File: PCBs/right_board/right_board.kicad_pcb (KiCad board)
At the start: 2 copper layers, 143.8 x 139.6 mm, 98 parts, among them J101 USB4510-03-1-A, J102 Conn_ARM_SWD_TagConnect_TC2030, J103 GSB12J21C1EU, J104 USB4510-03-1-A, SW101 SW_DIP_x01, SW102 SW_DIP_x01, SW103 SW_DIP_x01, SW104 SW_DIP_x01, SW105 SW_DIP_x01, SW106 SW_DIP_x01, SW107 SW_DIP_x01, SW108 SW_DIP_x01, SW109 SW_DIP_x01, SW110 SW_DIP_x01, SW111 SW_DIP_x01, SW112 SW_DIP_x01, SW113 SW_DIP_x01, SW114 SW_DIP_x01, SW115 SW_DIP_x01, SW116 SW_DIP_x01, SW117 SW_DIP_x01, SW118 SW_DIP_x01, SW119 SW_DIP_x01, SW120 SW_DIP_x01, SW121 SW_DIP_x01, SW122 SW_DIP_x01, SW123 SW_DIP_x01, SW124 SW_DIP_x01, SW125 SW_DIP_x01, SW126 SW_DIP_x01, SW127 SW_DIP_x01, SW128 RIC11-31S15.5D7-TH, U101 STM32G0C1CEUx, U102 USB2533-1080AEN, U103 M24256X-FCU6T_VF, U104 USBLC6-4SC6, U105 USBLC6-4SC6, U106 USBLC6-4SC6, Y101 CX2016SA24000D0HLLG3

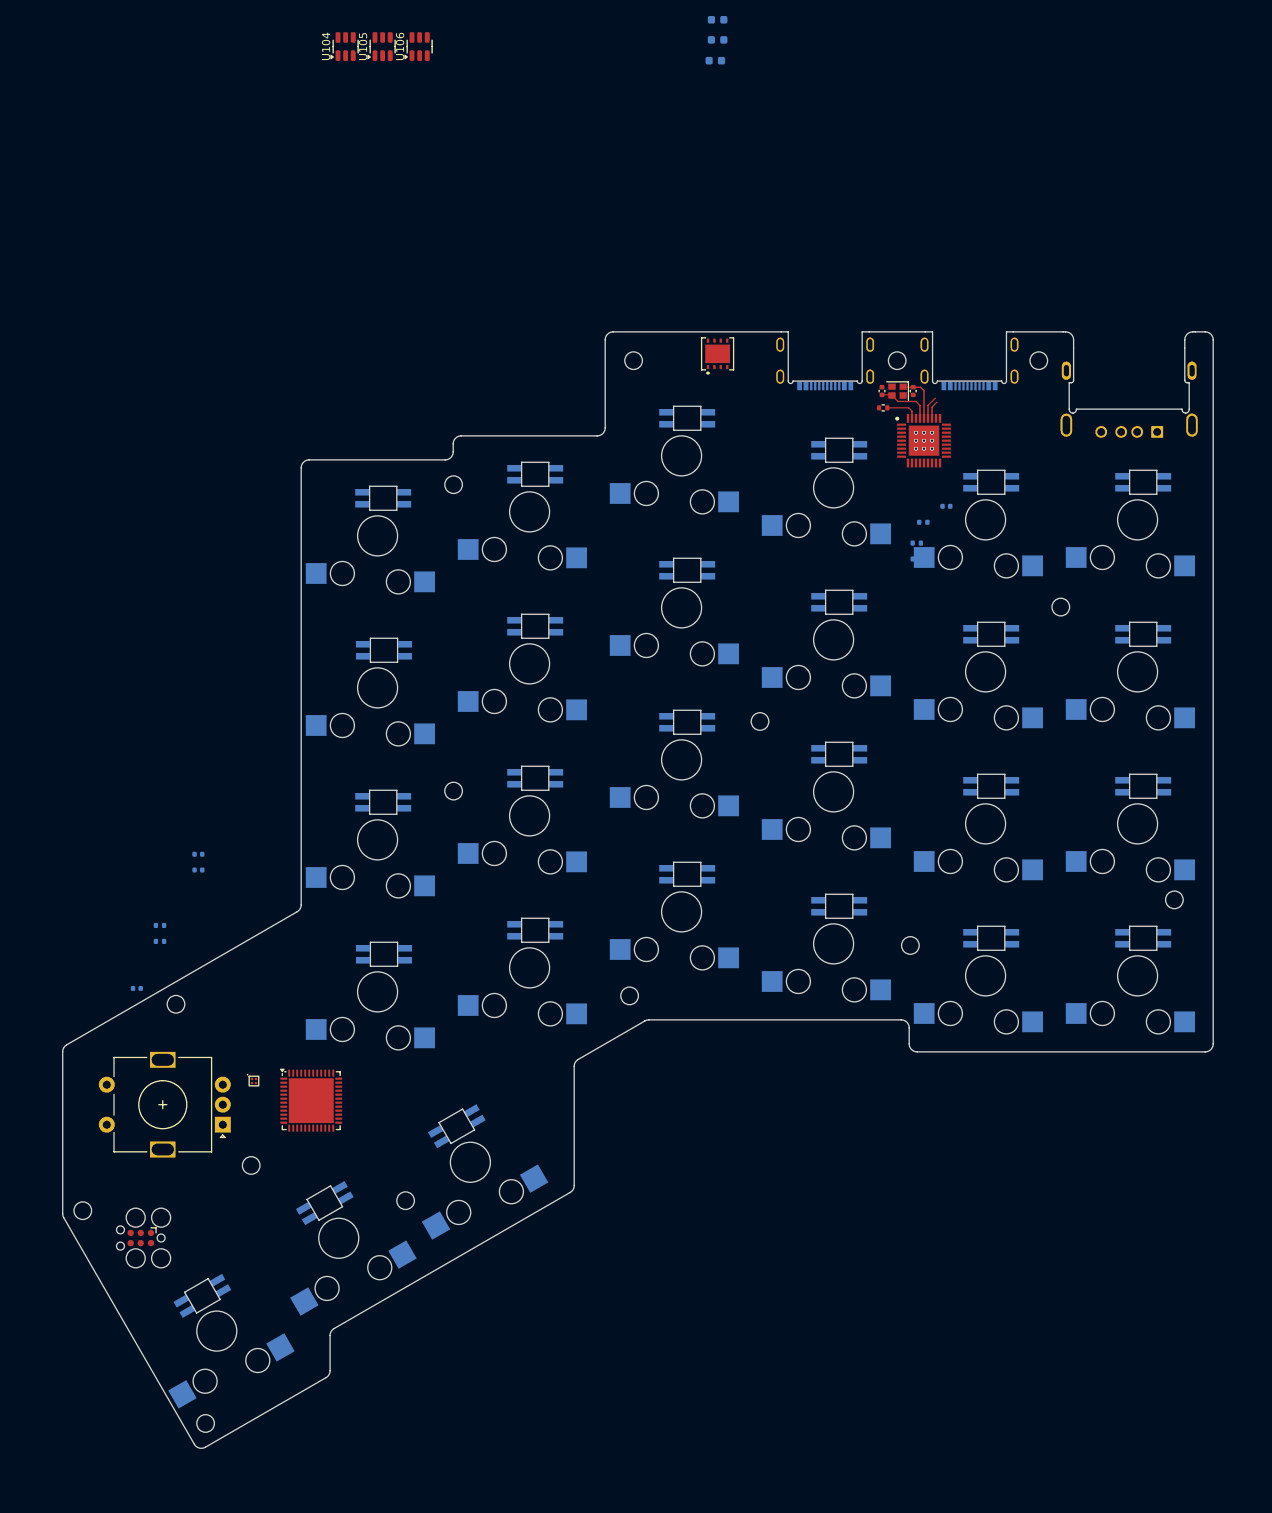
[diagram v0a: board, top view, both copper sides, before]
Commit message: Right board done, all components ordered
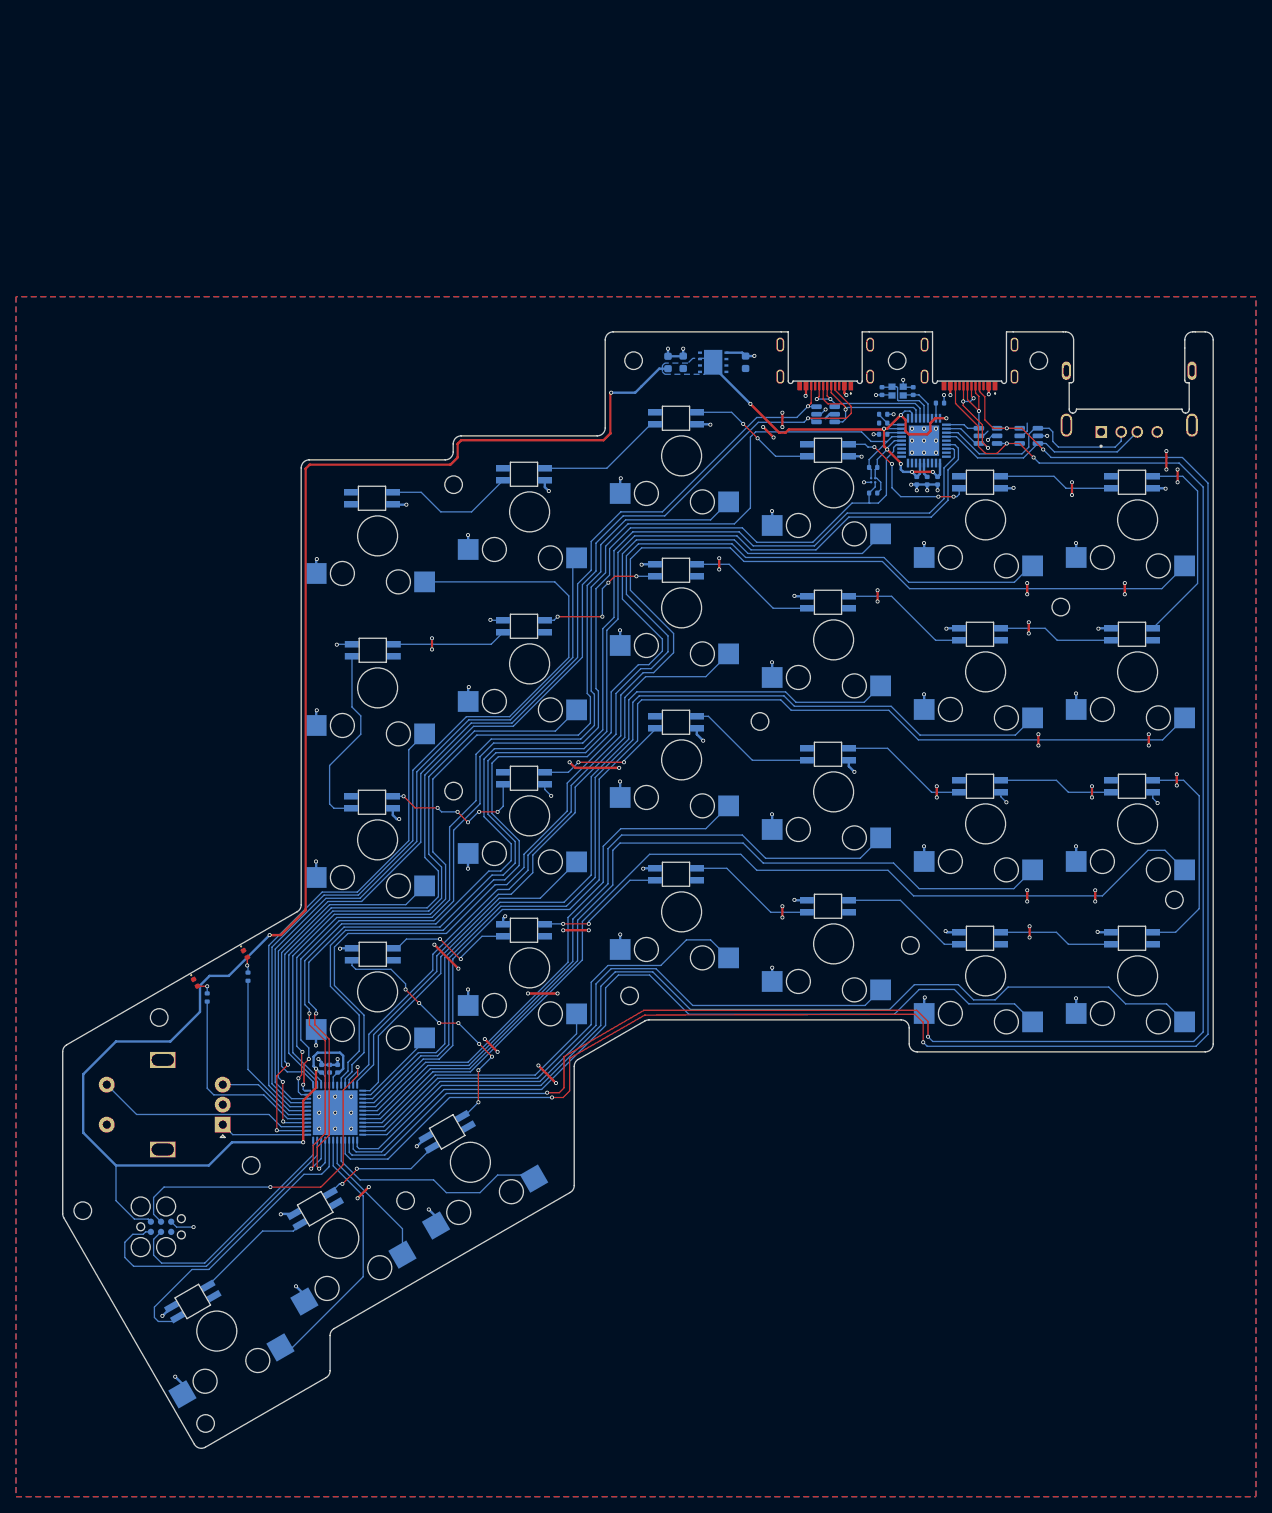
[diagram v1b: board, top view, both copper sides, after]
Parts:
- added C105: 1u, Capacitor_SMD:C_0402_1005Metric, B.Cu at (180.2, 58.0)
- added C106: 100n, Capacitor_SMD:C_0402_1005Metric, B.Cu at (177.6, 58.0)
- added D128: WHITE, LED_SMD:LED_0402_1005Metric, F.Cu at (93.7, 117.2)
- added D129: WHITE, LED_SMD:LED_0402_1005Metric, F.Cu at (87.4, 120.8)
- added R106: 3k3, Resistor_SMD:R_0402_1005Metric, B.Cu at (94.0, 120.0)
- added R107: 3k3, Resistor_SMD:R_0402_1005Metric, B.Cu at (88.9, 122.6)
- C102, C103, J102, PS101, R103, U101, U102, U103, U104, U105, U106, Y101: moved to B.Cu
- J101, J103, J104, REF**: moved to F.Cu
- moved SW121 153.4 mm to (205.2, 62.9), turned to 0 degrees
- moved D101 111.9 mm to (87.1, 160.6), turned to 30 degrees
- moved D118 108.3 mm to (147.5, 69.2), turned to 0 degrees
- moved U103 107.8 mm to (172.1, 57.9), turned to 180 degrees
- moved R102 107.0 mm to (172.1, 56.3)
- moved D109 106.2 mm to (204.5, 115.2), turned to 0 degrees
- moved SW126 105.9 mm to (90.1, 164.3), turned to 30 degrees
- moved R101 104.3 mm to (172.1, 59.5)
- moved SW114 97.1 mm to (167.2, 77.9), turned to 0 degrees
- moved SW101 95.0 mm to (110.2, 64.9)
- moved U106 90.4 mm to (191.6, 52.4), turned to 180 degrees
- moved U105 90.0 mm to (186.5, 52.4), turned to 180 degrees
- moved D102 89.2 mm to (102.4, 149.0), turned to 30 degrees
- moved D125 87.4 mm to (147.5, 50.2)
- moved D126 82.3 mm to (128.5, 57.2)
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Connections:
- R101 pad 1: +3V3 -> +3.3V
- R102 pad 1: +3V3 -> +3.3V
- SW106 pad 2: /KEY_B3 -> /KEY_B2
- SW107 pad 2: /KEY_C3 -> /KEY_C2
- SW108 pad 2: /KEY_D3 -> /KEY_D2
- SW126 pad 2: /KEY_E2 -> /KEY_E3
- SW127 pad 2: /KEY_E3 -> /KEY_E2
- U101 pad 1: unconnected-(U101-PC13-Pad1) -> /KEY_C1
- U101 pad 11: unconnected-(U101-PA0-Pad11) -> /KEY_A6
- U101 pad 12: unconnected-(U101-PA1-Pad12) -> /KEY_B3
- U101 pad 13: unconnected-(U101-PA2-Pad13) -> /KEY_C2
- U101 pad 14: unconnected-(U101-PA3-Pad14) -> /KEY_D1
- U101 pad 15: unconnected-(U101-PA4-Pad15) -> /KEY_B4
- U101 pad 16: unconnected-(U101-PA5-Pad16) -> /KEY_B5
- U101 pad 17: unconnected-(U101-PA6-Pad17) -> /KEY_B6
- U101 pad 18: unconnected-(U101-PA7-Pad18) -> /KEY_C3
- U101 pad 19: unconnected-(U101-PB0-Pad19) -> /KEY_C4
- U101 pad 2: unconnected-(U101-PC14-Pad2) -> /KEY_B2
- U101 pad 20: unconnected-(U101-PB1-Pad20) -> /KEY_C5
- U101 pad 21: unconnected-(U101-PB2-Pad21) -> /KEY_C6
- U101 pad 22: unconnected-(U101-PB10-Pad22) -> /KEY_D2
- U101 pad 23: unconnected-(U101-PB11-Pad23) -> /KEY_D3
- U101 pad 24: unconnected-(U101-PB12-Pad24) -> /KEY_D4
- U101 pad 25: unconnected-(U101-PB13-Pad25) -> /KEY_D6
- U101 pad 26: unconnected-(U101-PB14-Pad26) -> /KEY_D5
- U101 pad 29: unconnected-(U101-PA9/UCPD1_DBCC1-Pad29) -> /KEY_E1
- U101 pad 3: unconnected-(U101-PC15-Pad3) -> /KEY_A3
- U101 pad 30: unconnected-(U101-PC6-Pad30) -> /KEY_E2
- U101 pad 31: unconnected-(U101-PC7-Pad31) -> /KEY_E3
- U101 pad 32: unconnected-(U101-PA10/UCPD1_DBCC2-Pad32) -> /LED1
- U101 pad 37: unconnected-(U101-PA15-Pad37) -> /ENC_A
- U101 pad 39: unconnected-(U101-PD1-Pad39) -> /ENC_SW
- U101 pad 4: +3V3 -> +3.3V
- U101 pad 41: unconnected-(U101-PD3-Pad41) -> /STAT2
- U101 pad 42: unconnected-(U101-PB3-Pad42) -> /ENC_B
- U101 pad 43: unconnected-(U101-PB4-Pad43) -> /STAT1
- U101 pad 44: unconnected-(U101-PB5-Pad44) -> /KEY_B1
- U101 pad 45: unconnected-(U101-PB6-Pad45) -> /KEY_A1
- U101 pad 46: unconnected-(U101-PB7-Pad46) -> /KEY_A2
- U101 pad 47: unconnected-(U101-PB8-Pad47) -> /SCL
- U101 pad 48: unconnected-(U101-PB9-Pad48) -> /SDA
- U101 pad 6: +3V3 -> +3.3V
- U101 pad 8: unconnected-(U101-PF0-Pad8) -> /KEY_A4
- U101 pad 9: unconnected-(U101-PF1-Pad9) -> /KEY_A5
- U102 pad 10: +3V3 -> +3.3V
- U102 pad 15: +3V3 -> +3.3V
- U102 pad 23: +3V3 -> +3.3V
- U102 pad 26: +3V3 -> +3.3V
- U102 pad 29: +3V3 -> +3.3V
- U102 pad 36: +3V3 -> +3.3V
- U103 pad A1: +3V3 -> +3.3V
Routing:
- net +3.3V: track 0.00 -> 285.1 mm, vias 0 -> 12
- net /USB1_CC2: track 0.00 -> 229.9 mm, vias 0 -> 4
- net /USB1_CC1: track 0.00 -> 228.4 mm, vias 0 -> 4
- net /USB3_DN: track 0.00 -> 170.2 mm, vias 0 -> 2
- net /USB3_DP: track 0.00 -> 169.4 mm, vias 0 -> 2
- net /KEY_A6: track 0.00 -> 159.3 mm
- net /SCL: track 0.00 -> 154.3 mm, vias 0 -> 2
- net /KEY_A5: track 0.00 -> 151.1 mm
- net /USB0_CC1: track 0.00 -> 149.6 mm, vias 0 -> 3
- net /SDA: track 0.00 -> 147.9 mm, vias 0 -> 2
- net /KEY_B6: track 0.00 -> 143.4 mm
- net /KEY_A4: track 0.00 -> 141.0 mm
- net /USB0_CC2: track 0.00 -> 135.4 mm, vias 0 -> 3
- net GND: track 0.00 -> 132.3 mm, vias 9 -> 91
- net /KEY_C6: track 0.00 -> 125.0 mm
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- added copper zone on B.Cu, net +3.3V
- added copper zone on F.Cu, net GND
- added copper zone on B.Cu, net VBUS

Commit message: Pinout updates
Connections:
- net /KEY_A1 renamed /KEY_A7
- net /KEY_A2 renamed /KEY_A8
- net /KEY_A3 renamed /KEY_A9
- net /KEY_A4 renamed /KEY_A10
- net /KEY_A5 renamed /KEY_A11
- net /KEY_A6 renamed /KEY_A12
- net /KEY_B1 renamed /KEY_B7
- net /KEY_B2 renamed /KEY_B8
- net /KEY_B3 renamed /KEY_B9
- net /KEY_B4 renamed /KEY_B10
- net /KEY_B5 renamed /KEY_B11
- net /KEY_B6 renamed /KEY_B12
- net /KEY_C1 renamed /KEY_C7
- net /KEY_C2 renamed /KEY_C8
- net /KEY_C3 renamed /KEY_C9
- net /KEY_C4 renamed /KEY_C10
- net /KEY_C5 renamed /KEY_C11
- net /KEY_C6 renamed /KEY_C12
- net /KEY_D1 renamed /KEY_D7
- net /KEY_D2 renamed /KEY_D8
- net /KEY_D3 renamed /KEY_D9
- net /KEY_D4 renamed /KEY_D10
- net /KEY_D5 renamed /KEY_D11
- net /KEY_D6 renamed /KEY_D12
- net /KEY_E1 renamed /KEY_E6
- net /KEY_E2 renamed /KEY_E5
- net /KEY_E3 renamed /KEY_E4
